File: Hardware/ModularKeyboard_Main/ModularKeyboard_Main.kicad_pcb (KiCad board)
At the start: 2 copper layers, 50 parts, among them J1 Conn_01x03, J2 Conn_01x03, J3 SM04B-SRSS-TB(LF)(SN), SW0 SW_SPST, SW1 SW_SPST, SW10 SW_SPST, SW11 SW_SPST, SW12 SW_SPST, SW13 SW_SPST, SW14 SW_SPST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

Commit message: Completed most wiring
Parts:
- added H1: MountingHole, MountingHole:MountingHole_2.2mm_M2, F.Cu at (196.3, 95.1)
- added H2: MountingHole, MountingHole:MountingHole_2.2mm_M2, F.Cu at (196.3, 133.2)
- added H3: MountingHole, MountingHole:MountingHole_2.2mm_M2, F.Cu at (158.2, 95.1)
- added H4: MountingHole, MountingHole:MountingHole_2.2mm_M2, F.Cu at (158.2, 133.2)
- added J3: Conn_01x03, CUSTOM:PG-3P-2.5, F.Cu at (140.4, 74.2)
- added J4: Conn_01x03, CUSTOM:PG-3P-2.5, F.Cu at (213.4, 58.1)
- added J6: SM04B-SRSS-TB(LF)(SN), SM04B-SRSS-TB_LF__SN:JST_SM04B-SRSS-TB(LF)(SN), B.Cu at (146.8, 73.2)
- added OL1: OLED, kbd-master:OLED_v2, F.Cu at (194.9, 62.0)
- added R6: DNP, Resistor_SMD:R_0402_1005Metric, B.Cu at (164.0, 69.0)
- added R7: DNP, Resistor_SMD:R_0402_1005Metric, B.Cu at (143.5, 69.0)
- moved C8 55.7 mm to (152.1, 70.5), turned to 0 degrees
- moved SW16 50.1 mm to (153.6, 73.9)
- moved R1 47.3 mm to (152.1, 71.6)
- moved J1 7.41 mm to (213.4, 65.5)
- moved RN2 5.64 mm to (197.9, 71.1), turned to 180 degrees
- moved U1 5.56 mm to (200.6, 64.2)
- moved RN4 3.40 mm to (206.6, 73.8), turned to 180 degrees
- moved RN3 3.08 mm to (206.6, 71.1), turned to 180 degrees
- moved J2 3.04 mm to (140.4, 66.2)
- moved U3 2.84 mm to (209.3, 64.2)
- moved RN1 1.68 mm to (197.9, 73.8), turned to 180 degrees
- moved C1 1.44 mm to (147.2, 68.3), turned to 180 degrees
- moved MH3 0.74 mm to (170.2, 69.1)
- moved MH4 0.74 mm to (184.2, 69.1)
- moved MH1 0.74 mm to (170.2, 56.6)
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- renumbered J3 to J5
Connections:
- net Net-(R2-Pad1) renamed /MCU_D-
- net Net-(R3-Pad1) renamed /MCU_D+
- J1 pad 1: /SCLK -> SPI1_SCK
- J2 pad 1: /~{SS} -> PL
- J2 pad 2: /MISO -> CE
- J2 pad 3: /MOSI -> SPI1_MISO
- J5 pad S1: unconnected-(J3-PadS1) -> Net-(J5-PadS1)
- J5 pad S2: unconnected-(J3-PadS1) -> Net-(J5-PadS1)
- U1 pad 1: ~{PL} -> PL
- U1 pad 15: ~{CE} -> CE
- U2 pad 26: unconnected-(U2-Pad26) -> SPI2_SCK
- U2 pad 27: unconnected-(U2-Pad27) -> SPI2_MISO
- U2 pad 28: unconnected-(U2-Pad28) -> SPI2_MOSI
- U2 pad 34: SPI2_SCK -> SWDIO
- U2 pad 37: SPI2_MISO -> SWCLK
- U2 pad 38: SPI2_MOSI -> unconnected-(U2-Pad38)
- U2 pad 39: unconnected-(U2-Pad39) -> PL
- U2 pad 40: unconnected-(U2-Pad40) -> CE
- U2 pad 42: unconnected-(U2-Pad42) -> I2C1_SCL
- U2 pad 43: unconnected-(U2-Pad43) -> I2C1_SDA
- U3 pad 1: ~{PL} -> PL
- U3 pad 15: ~{CE} -> CE
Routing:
- net +3V3: track 0.00 -> 161.5 mm
- net GND: track 0.00 -> 31.6 mm, vias 0 -> 25
- net PL: track 0.00 -> 24.9 mm
- net SWDIO: track 0.00 -> 20.4 mm
- net R0_SW_0: track 0.00 -> 14.3 mm
- net R1_SW_4: track 0.00 -> 14.3 mm
- net R0_SW_1: track 0.00 -> 13.6 mm
- net R1_SW_5: track 0.00 -> 13.6 mm
- net NRST: track 0.00 -> 13.5 mm, vias 0 -> 2
- net R0_SW_2: track 0.00 -> 13.2 mm
- net R1_SW_6: track 0.00 -> 12.9 mm
- net R0_SW_3: track 0.00 -> 12.1 mm
- net R1_SW_7: track 0.00 -> 12.1 mm
- net R1_SW_3: track 0.00 -> 12.0 mm
- net R0_SW_7: track 0.00 -> 12.0 mm
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- added copper zone on B.Cu, net VCC

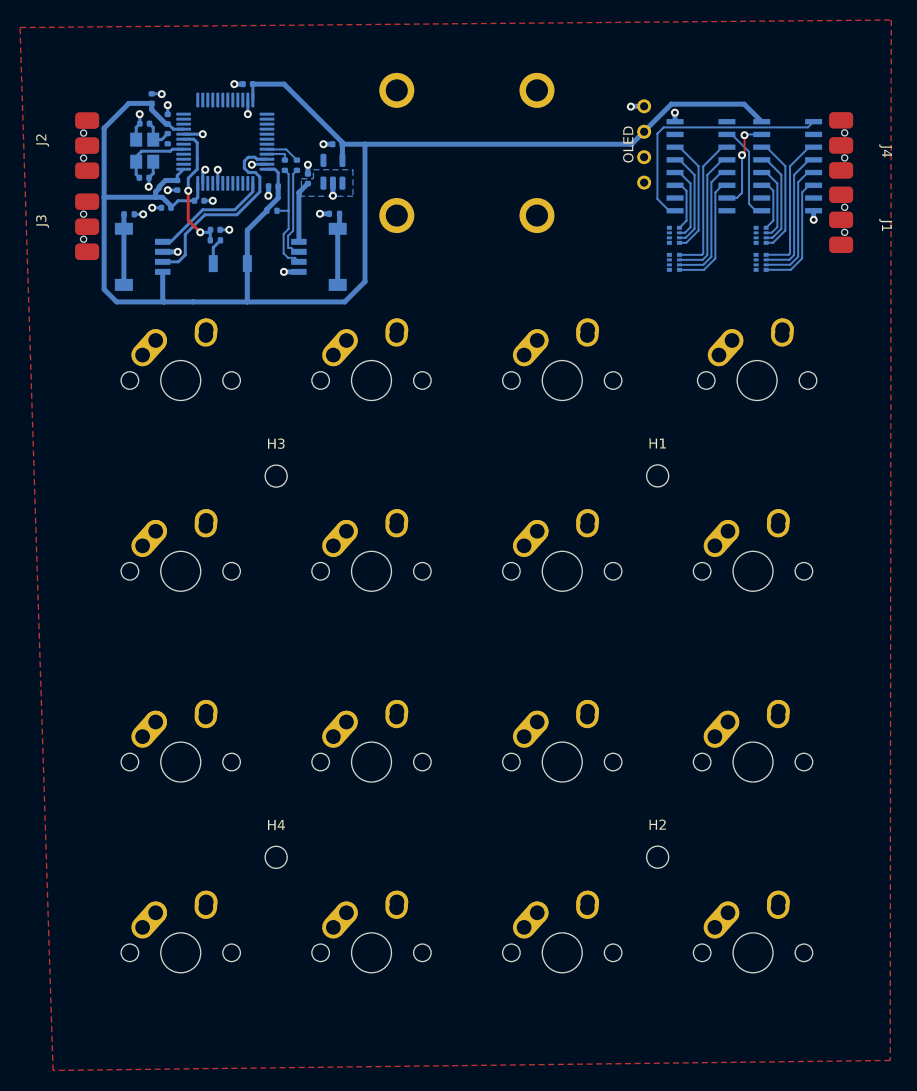
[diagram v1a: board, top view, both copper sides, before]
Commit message: Completed wiring v0.1 -- add bom
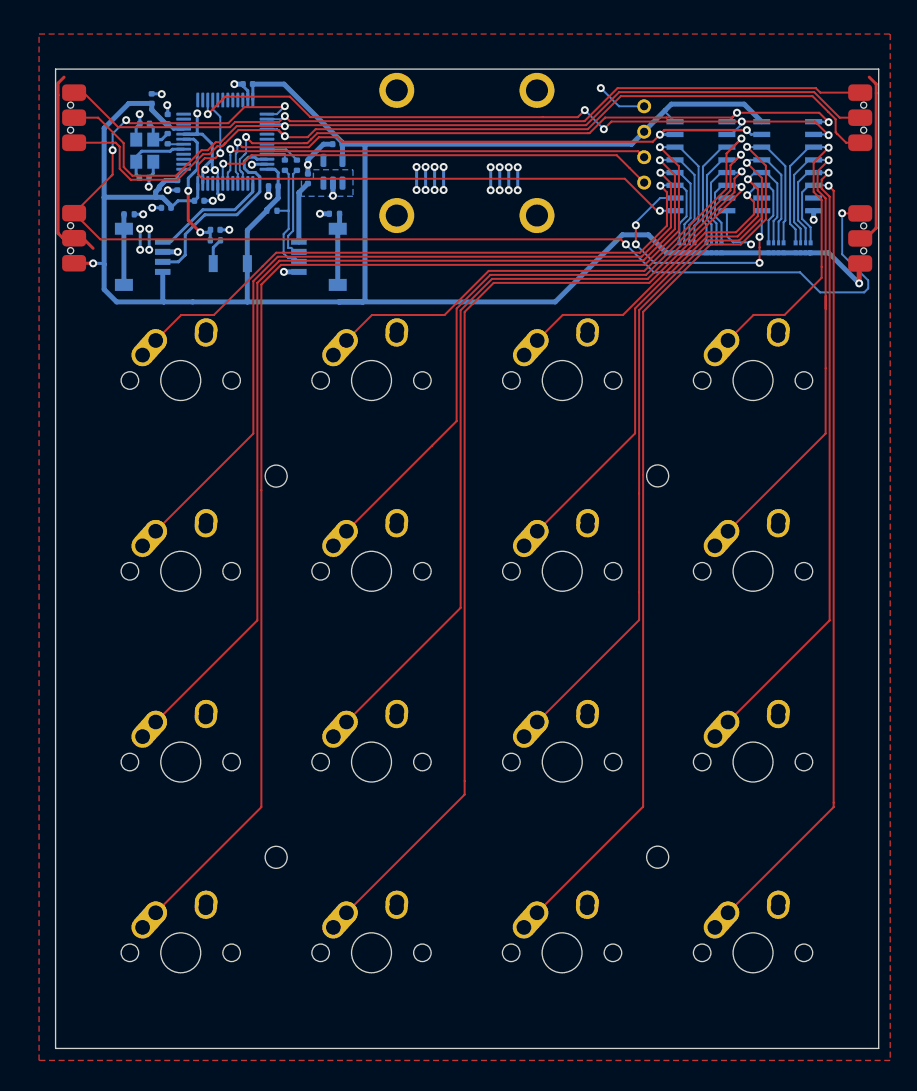
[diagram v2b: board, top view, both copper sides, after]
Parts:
- moved SW3 81.1 mm to (148.7, 142.8)
- moved SW12 80.8 mm to (205.8, 85.6)
- moved SW7 53.9 mm to (167.7, 142.8)
- moved SW2 53.9 mm to (148.7, 123.7)
- moved SW8 53.9 mm to (186.8, 85.6)
- moved SW13 53.9 mm to (205.8, 104.7)
- moved SW11 27.0 mm to (186.7, 142.8)
- moved SW1 26.9 mm to (148.7, 104.7)
- moved SW6 26.9 mm to (167.7, 123.7)
- moved SW4 26.9 mm to (167.7, 85.6)
- moved SW14 26.9 mm to (205.8, 123.7)
- moved SW9 26.9 mm to (186.8, 104.7)
- moved RN4 4.44 mm to (210.8, 72.3), turned to -90 degrees
- moved RN2 4.14 mm to (201.9, 72.3), turned to -90 degrees
- moved J4 3.36 mm to (215.3, 55.3)
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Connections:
- J1 pad 1: SPI1_SCK -> SPI2_CS
- J2 pad 1: PL -> SPI2_MOSI
- J2 pad 2: CE -> SPI2_MISO
- J2 pad 3: SPI1_MISO -> SPI2_SCK
- J3 pad 3: SPI1_SCK -> SPI2_CS
- J4 pad 1: SPI1_MISO -> SPI2_SCK
- J4 pad 2: CE -> SPI2_MISO
- J4 pad 3: PL -> SPI2_MOSI
- U2 pad 25: unconnected-(U2-Pad25) -> SPI2_CS
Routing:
- net SPI2_CS: track 0.00 -> 123.4 mm, vias 0 -> 5
- net R0_SW_3: track 12.1 -> 132.6 mm, vias 0 -> 1
- net R0_SW_2: track 13.2 -> 110.6 mm, vias 0 -> 1
- net R0_SW_7: track 12.0 -> 106.2 mm, vias 0 -> 1
- net SPI2_MOSI: track 0.00 -> 90.8 mm, vias 0 -> 1
- net R1_SW_3: track 12.0 -> 100.9 mm, vias 0 -> 1
- net SPI2_MISO: track 0.00 -> 88.7 mm, vias 0 -> 1
- net SPI2_SCK: track 0.00 -> 84.1 mm, vias 0 -> 1
- net GND: track 31.6 -> 114.0 mm, vias 25 -> 44
- net R0_SW_6: track 9.84 -> 89.6 mm, vias 0 -> 1
- net R0_SW_1: track 13.6 -> 88.4 mm, vias 0 -> 1
- net R1_SW_7: track 12.1 -> 85.5 mm, vias 0 -> 1
- net SPI1_SCK: track 0.00 -> 71.1 mm, vias 0 -> 5
- net R1_SW_2: track 9.85 -> 78.6 mm, vias 0 -> 1
- net R0_SW_5: track 7.70 -> 74.2 mm, vias 0 -> 1
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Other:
- board outline added: 82.2 x 97.8 mm
- board text added: "bsc v0.1 9/22"
- board text added: "初"

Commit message: Completed v0.1
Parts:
- C11: value DNP -> 2.2uF
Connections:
- J6 pad 2: SWDIO -> SWCLK
- J6 pad 4: SWCLK -> SWDIO
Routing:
- net SWCLK: track 11.9 -> 17.3 mm
- net SWDIO: track 20.4 -> 18.4 mm
- net GND: track 114.0 -> 115.9 mm, vias 44 -> 46
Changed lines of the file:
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@@
       (outputformat 1)
       (mirror false)
-      (drillshape 1)
+      (drillshape 0)
       (scaleselection 1)
-      (outputdirectory "")
+      (outputdirectory "_Production/Gerbers/")
     )
   )
@@
       (effects (font (size 0.25 0.25) (thickness 0.0625)) (justify mirror))
     )
-    (fp_text value "DNP" (at 0 -1.16 90) (layer "B.Fab")
+    (fp_text value "2.2uF" (at 0 -1.16 90) (layer "B.Fab")
       (effects (font (size 1 1) (thickness 0.15)) (justify mirror))
     )
@@
       (net 1 "+3V3") (pinfunction "1") (pintype "passive"))
     (pad "2" smd rect locked (at -0.5 0 90) (size 0.6 1.55) (layers "B.Cu" "B.Paste" "B.Mask")
-      (net 10 "SWDIO") (pinfunction "2") (pintype "passive"))
+      (net 11 "SWCLK") (pinfunction "2") (pintype "passive"))
     (pad "3" smd rect locked (at 0.5 0 90) (size 0.6 1.55) (layers "B.Cu" "B.Paste" "B.Mask")
       (net 2 "GND") (pinfunction "3") (pintype "passive"))
     (pad "4" smd rect locked (at 1.5 0 90) (size 0.6 1.55) (layers "B.Cu" "B.Paste" "B.Mask")
-      (net 11 "SWCLK") (pinfunction "4") (pintype "passive"))
+      (net 10 "SWDIO") (pinfunction "4") (pintype "passive"))
     (pad "S1" smd rect locked (at -2.8 -3.875 270) (size 1.2 1.8) (layers "B.Cu" "B.Paste" "B.Mask")
       (net 34 "Net-(J6-PadS1)") (pinfunction "SHIELD") (pintype "passive"))
@@
   (via (at 190.6 56.4) (size 0.8) (drill 0.4) (layers "F.Cu" "B.Cu") (net 2))
   (via (at 146.75 57) (size 0.8) (drill 0.4) (layers "F.Cu" "B.Cu") (net 2))
+  (via (at 154.4 72.55) (size 0.8) (drill 0.4) (layers "F.Cu" "B.Cu") (net 2))
   (via (at 174 64.275) (size 0.8) (drill 0.4) (layers "F.Cu" "B.Cu") (net 2))
+  (via (at 156.8 70.45) (size 0.8) (drill 0.4) (layers "F.Cu" "B.Cu") (free) (net 2))
   (via (at 144.55 59) (size 0.8) (drill 0.4) (layers "F.Cu" "B.Cu") (net 2))
   (via (at 155.75 64.05) (size 0.8) (drill 0.4) (layers "F.Cu" "B.Cu") (net 2))
   (via (at 151.1 64.55) (size 0.8) (drill 0.4) (layers "F.Cu" "B.Cu") (net 2))
+  (via (at 156.8 72.55) (size 0.8) (drill 0.4) (layers "F.Cu" "B.Cu") (net 2))
   (via (at 181.4 64.3) (size 0.8) (drill 0.4) (layers "F.Cu" "B.Cu") (net 2))
   (via (at 145.45 66.25) (size 0.8) (drill 0.4) (layers "F.Cu" "B.Cu") (net 2))
   (via (at 162.55 68.95) (size 0.8) (drill 0.4) (layers "F.Cu" "B.Cu") (net 2))
   (via (at 172.2 66.575) (size 0.8) (drill 0.4) (layers "F.Cu" "B.Cu") (net 2))
-  (via (at 145.5 70.45) (size 0.8) (drill 0.4) (layers "F.Cu" "B.Cu") (free) (net 2))
   (via (at 152.074484 64.592272) (size 0.8) (drill 0.4) (layers "F.Cu" "B.Cu") (net 2))
   (via (at 174 66.575) (size 0.8) (drill 0.4) (layers "F.Cu" "B.Cu") (net 2))
   (via (at 148.35 72.75) (size 0.8) (drill 0.4) (layers "F.Cu" "B.Cu") (net 2))
+  (via (at 154.4 70.45) (size 0.8) (drill 0.4) (layers "F.Cu" "B.Cu") (free) (net 2))
   (via (at 144.9 69) (size 0.8) (drill 0.4) (layers "F.Cu" "B.Cu") (net 2))
   (via (at 174.9 66.575) (size 0.8) (drill 0.4) (layers "F.Cu" "B.Cu") (net 2))
@@
   (via (at 163.85 67.15) (size 0.8) (drill 0.4) (layers "F.Cu" "B.Cu") (net 2))
   (via (at 161.35 64.05) (size 0.8) (drill 0.4) (layers "F.Cu" "B.Cu") (net 2))
-  (via (at 145.5 72.55) (size 0.8) (drill 0.4) (layers "F.Cu" "B.Cu") (net 2))
   (segment (start 150.85 64.8) (end 151.1 64.55) (width 0.3) (layer "B.Cu") (net 2))
   (segment (start 211.84933 68.645) (end 211.84933 69.5408) (width 0.5) (layer "B.Cu") (net 2))
@@
   (segment (start 150.8 61) (end 151.8 62) (width 0.3) (layer "B.Cu") (net 2))
   (segment (start 150.3 58.9245) (end 150.3 61) (width 0.3) (layer "B.Cu") (net 2))
-  (segment (start 145.5 70.65) (end 145.5 72.55) (width 0.3) (layer "B.Cu") (net 2))
   (segment (start 181.4 66.6) (end 181.4 64.3) (width 0.3) (layer "B.Cu") (net 2))
   (segment (start 145.9 64.93) (end 145.48 65.35) (width 0.3) (layer "B.Cu") (net 2))
@@
   (segment (start 151.142272 64.592272) (end 151.1 64.55) (width 0.2) (layer "B.Cu") (net 2))
   (segment (start 203.8 71.8) (end 205.4 71.8) (width 0.2) (layer "B.Cu") (net 2))
+  (segment (start 154.4 70.65) (end 154.4 72.55) (width 0.3) (layer "B.Cu") (net 2))
   (segment (start 146.85 72.75) (end 148.35 72.75) (width 0.5) (layer "B.Cu") (net 2))
   (segment (start 152.35 66.95) (end 152.35 65.9125) (width 0.3) (layer "B.Cu") (net 2))
@@
   (segment (start 155.35 57.5875) (end 155.35 56.675) (width 0.3) (layer "B.Cu") (net 2))
   (segment (start 211.84933 69.5408) (end 211.85853 69.55) (width 0.5) (layer "B.Cu") (net 2))
+  (segment (start 156.8 70.65) (end 156.8 72.55) (width 0.3) (layer "B.Cu") (net 2))
   (segment (start 151.8 62) (end 151.8 63.5) (width 0.3) (layer "B.Cu") (net 2))
   (segment (start 152.7 67.3) (end 152.35 66.95) (width 0.3) (layer "B.Cu") (net 2))
@@
   (segment (start 164.325 76.05) (end 164.325 70.45) (width 0.5) (layer "B.Cu") (net 9))
   (segment (start 155.425 64.825) (end 156.101041 64.825) (width 0.3) (layer "B.Cu") (net 10))
-  (segment (start 148.410661 73.75) (end 146.85 73.75) (width 0.3) (layer "B.Cu") (net 10))
   (segment (start 156.060661 63.3) (end 155.4 63.3) (width 0.3) (layer "B.Cu") (net 10))
-  (segment (start 151.057106 69.05) (end 149.1 71.007106) (width 0.3) (layer "B.Cu") (net 10))
   (segment (start 156.55 65.273959) (end 156.55 66.758147) (width 0.3) (layer "B.Cu") (net 10))
-  (segment (start 154.258147 69.05) (end 151.057106 69.05) (width 0.3) (layer "B.Cu") (net 10))
   (segment (start 155 63.7) (end 155 64.4) (width 0.3) (layer "B.Cu") (net 10))
-  (segment (start 156.55 66.758147) (end 154.258147 69.05) (width 0.3) (layer "B.Cu") (net 10))
   (segment (start 157.2625 63.5) (end 156.260661 63.5) (width 0.3) (layer "B.Cu") (net 10))
+  (segment (start 148.8 69.8) (end 146.85 71.75) (width 0.3) (layer "B.Cu") (net 10))
   (segment (start 156.260661 63.5) (end 156.060661 63.3) (width 0.3) (layer "B.Cu") (net 10))
-  (segment (start 149.1 73.060661) (end 148.410661 73.75) (width 0.3) (layer "B.Cu") (net 10))
   (segment (start 155.4 63.3) (end 155 63.7) (width 0.3) (layer "B.Cu") (net 10))
-  (segment (start 149.1 71.007106) (end 149.1 73.060661) (width 0.3) (layer "B.Cu") (net 10))
+  (segment (start 153.508147 69.8) (end 148.8 69.8) (width 0.3) (layer "B.Cu") (net 10))
   (segment (start 155 64.4) (end 155.425 64.825) (width 0.3) (layer "B.Cu") (net 10))
+  (segment (start 156.55 66.758147) (end 153.508147 69.8) (width 0.3) (layer "B.Cu") (net 10))
   (segment (start 156.101041 64.825) (end 156.55 65.273959) (width 0.3) (layer "B.Cu") (net 10))
-  (segment (start 155.85 66.751041) (end 155.85 65.9125) (width 0.3) (layer "B.Cu") (net 11))
-  (segment (start 150.85 68.55) (end 154.051041 68.55) (width 0.3) (layer "B.Cu") (net 11))
-  (segment (start 147.65 71.75) (end 150.85 68.55) (width 0.3) (layer "B.Cu") (net 11))
-  (segment (start 154.051041 68.55) (end 155.85 66.751041) (width 0.3) (layer "B.Cu") (net 11))
-  (segment (start 146.85 71.75) (end 147.65 71.75) (width 0.3) (layer "B.Cu") (net 11))
+  (segment (start 155.85 66.751041) (end 153.301041 69.3) (width 0.3) (layer "B.Cu") (net 11))
+  (segment (start 146.05 73.75) (end 146.85 73.75) (width 0.3) (layer "B.Cu") (net 11))
+  (segment (start 145.6 73.3) (end 146.05 73.75) (width 0.3) (layer "B.Cu") (net 11))
+  (segment (start 155.85 65.9125) (end 155.85 66.751041) (width 0.3) (layer "B.Cu") (net 11))
+  (segment (start 153.301041 69.3) (end 146 69.3) (width 0.3) (layer "B.Cu") (net 11))
+  (segment (start 146 69.3) (end 145.6 69.7) (width 0.3) (layer "B.Cu") (net 11))
+  (segment (start 145.6 69.7) (end 145.6 73.3) (width 0.3) (layer "B.Cu") (net 11))
   (segment (start 159.875001 64.984999) (end 159.875001 70.649999) (width 0.2) (layer "B.Cu") (net 12))
   (segment (start 159.686397 72.35) (end 160.086397 72.75) (width 0.2) (layer "B.Cu") (net 12))
@@
   (segment (start 143.65 65.55) (end 142.5495 64.4495) (width 0.2) (layer "F.Cu") (net 62))
   (segment (start 213.319975 58.780025) (end 214.05 59.51005) (width 0.2) (layer "F.Cu") (net 62))
-  (segment (start 138.25 62.1) (end 138 61.85) (width 0.2) (layer "F.Cu") (net 62))
   (segment (start 189.3 60.5) (end 192.6 57.2) (width 0.2) (layer "F.Cu") (net 62))
   (segment (start 216.5 61.85) (end 215.08995 61.85) (width 0.2) (layer "F.Cu") (net 62))
